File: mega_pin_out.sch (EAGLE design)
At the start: 11 parts, among them X1 332-36

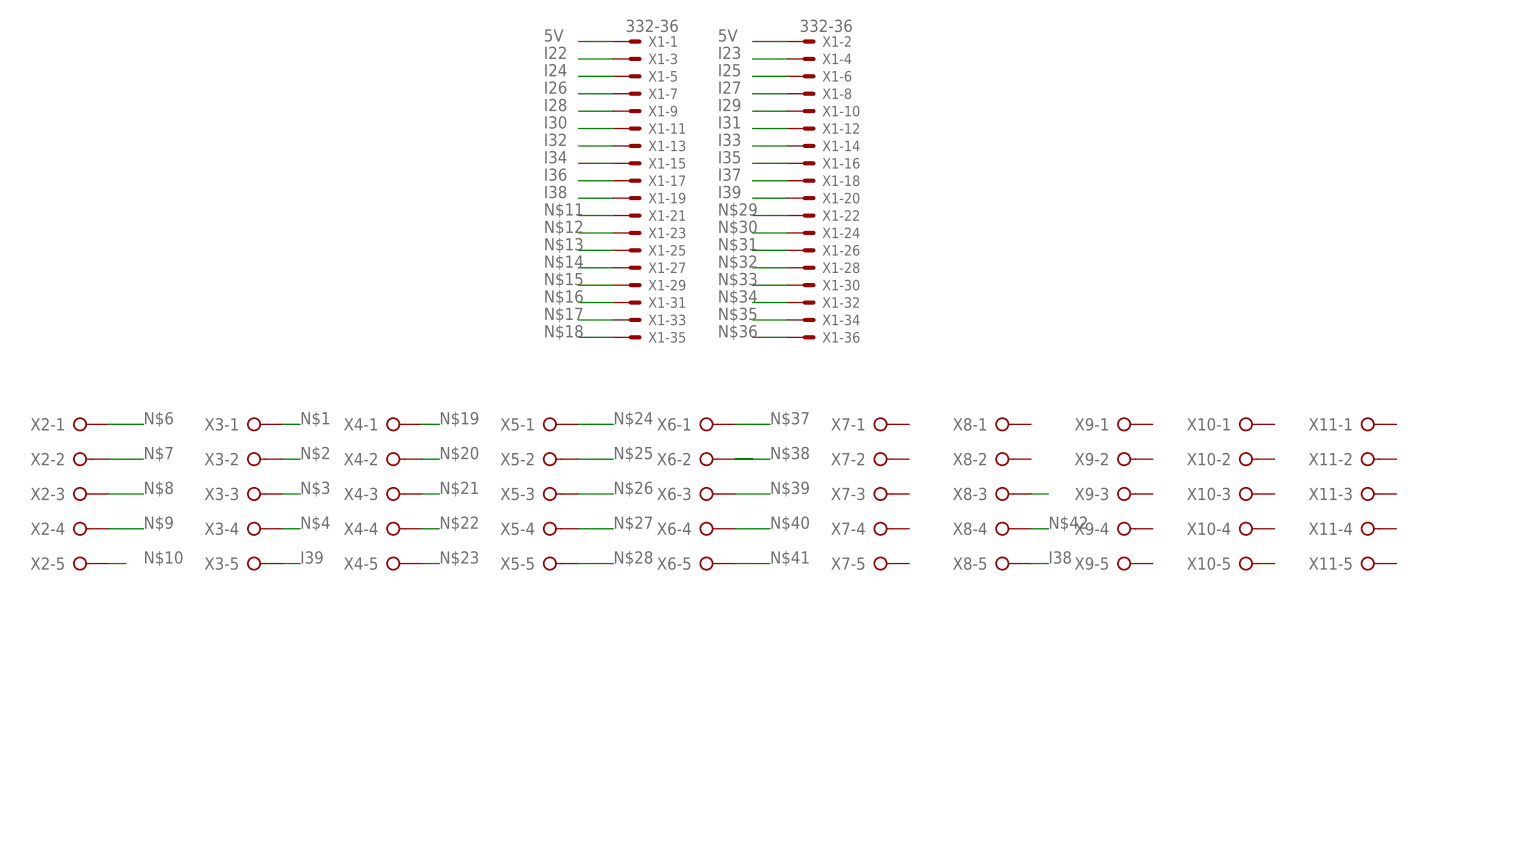
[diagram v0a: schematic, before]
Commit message: Full reroute of 2x18 female pins
- Fixed the female pins pcb layout part size
- Reroute all pins
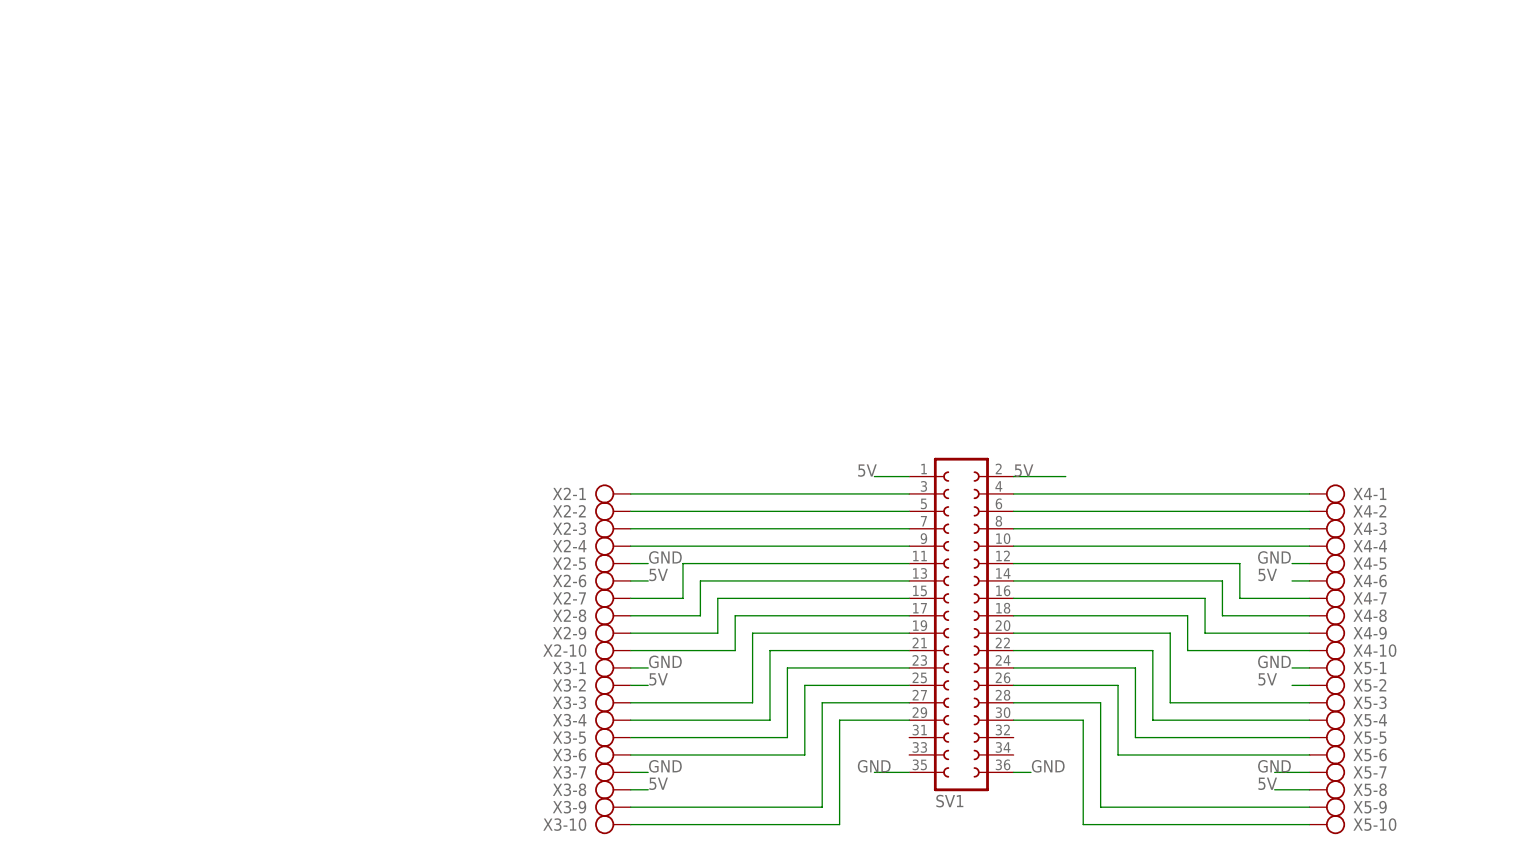
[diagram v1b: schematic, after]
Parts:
- removed X1: 332-36, con-garry:332-36
- removed X10, X11, X6, X7, X8, X9: (no value), con-wago-508:W237-05P
- added SV1: (no value), con-lsta:FE18-2
- X2, X3, X4, X5: device con-wago-508:W237-05P -> con-ptr500:AK500/10
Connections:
- removed net I22: X1-3.S
- removed net I23: X1-4.S
- removed net I24: X1-5.S
- removed net I25: X1-6.S
- removed net I26: X1-7.S
- removed net I27: X1-8.S
- removed net I28: X1-9.S
- removed net I29: X1-10.S
- removed net I30: X1-11.S
- removed net I32: X1-13.S
- removed net I34: X1-15.S
- removed net I36: X1-17.S
- removed net I37: X1-18.S
- removed net I38: X1-19.S, X8-5.KL
- removed net I39: X1-20.S, X3-5.KL
- removed net N$1: X3-1.KL
- removed net N$2: X3-2.KL
- removed net N$30: X1-24.S
- removed net N$31: X1-26.S
- removed net N$32: X1-28.S
- removed net N$33: X1-30.S
- removed net N$34: X1-32.S
- removed net N$35: X1-34.S
- removed net N$36: X1-36.S
- removed net N$37: X6-1.KL
- removed net N$38: X6-2.KL
- removed net N$39: X6-3.KL
- removed net N$40: X6-4.KL
- removed net N$41: X6-5.KL
- removed net N$42: X8-4.KL
- removed net N$43: X8-3.KL
- removed net N$6: X2-1.KL
- removed net N$7: X2-2.KL
- removed net N$8: X2-3.KL
- new net GND: SV1.35, SV1.36, X2-5.KL, X3-1.KL, X3-7.KL, X4-5.KL, X5-1.KL, X5-7.KL
- new net I47: SV1.27, X3-9.KL
- new net I49: SV1.29, X3-10.KL
- net 5V: now also SV1.1, SV1.2, X2-6.KL, X3-2.KL, X3-8.KL, X4-6.KL, X5-2.KL, X5-8.KL; no longer X1-1.S, X1-2.S
- net I31: now also SV1.11, X2-7.KL; no longer X1-12.S
- net I33: now also SV1.13, X2-8.KL; no longer X1-14.S
- net I35: now also SV1.15, X2-9.KL; no longer X1-16.S
- net N$10: now also SV1.9, X2-4.KL; no longer X2-5.KL
- net N$11: now also SV1.17, X2-10.KL; no longer X1-21.S
- net N$12: now also SV1.19, X3-3.KL; no longer X1-23.S
- net N$13: now also SV1.21, X3-4.KL; no longer X1-25.S
- net N$14: now also SV1.23, X3-5.KL; no longer X1-27.S
- net N$15: now also SV1.25, X3-6.KL; no longer X1-29.S
- net N$16: now also SV1.4, X4-1.KL; no longer X1-31.S
- net N$17: now also SV1.6, X4-2.KL; no longer X1-33.S
- net N$18: now also SV1.8, X4-3.KL; no longer X1-35.S
- net N$19: now also SV1.10, X4-4.KL; no longer X4-1.KL
- net N$20: now also SV1.12, X4-7.KL; no longer X4-2.KL
- net N$21: now also SV1.14, X4-8.KL; no longer X4-3.KL
- net N$22: now also SV1.16, X4-9.KL; no longer X4-4.KL
- net N$23: now also SV1.18, X4-10.KL; no longer X4-5.KL
- net N$24: now also SV1.20, X5-3.KL; no longer X5-1.KL
- net N$25: now also SV1.22, X5-4.KL; no longer X5-2.KL
- net N$26: now also SV1.24, X5-5.KL; no longer X5-3.KL
- net N$27: now also SV1.26, X5-6.KL; no longer X5-4.KL
- net N$28: now also SV1.28, X5-9.KL; no longer X5-5.KL
- net N$29: now also SV1.30, X5-10.KL; no longer X1-22.S
- net N$3: now also SV1.3, X2-1.KL; no longer X3-3.KL
- net N$4: now also SV1.5, X2-2.KL; no longer X3-4.KL
- net N$9: now also SV1.7, X2-3.KL; no longer X2-4.KL

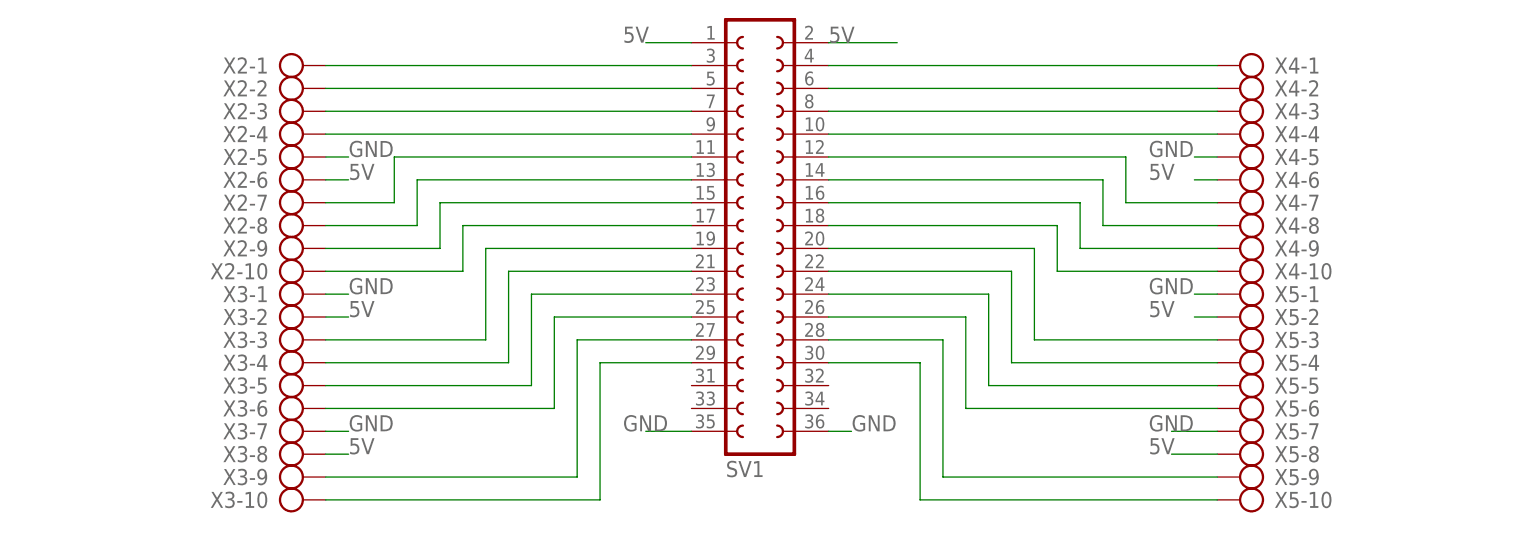
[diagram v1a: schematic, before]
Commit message: [BACK] Added capacitors for PIN 39 & 40 and others
* Schematic:
- Added text field for pin numbers name
- Added charging capacitors for pin 39 & 40 which are used as AC light state detectors. 

* Board
- Increased board layout from 100x80 to 100x85
- Increased clearance between terminal blocks to ~22.86 mm which was tested on breadboard to be easier during wiring. 
- Routed the capacitors
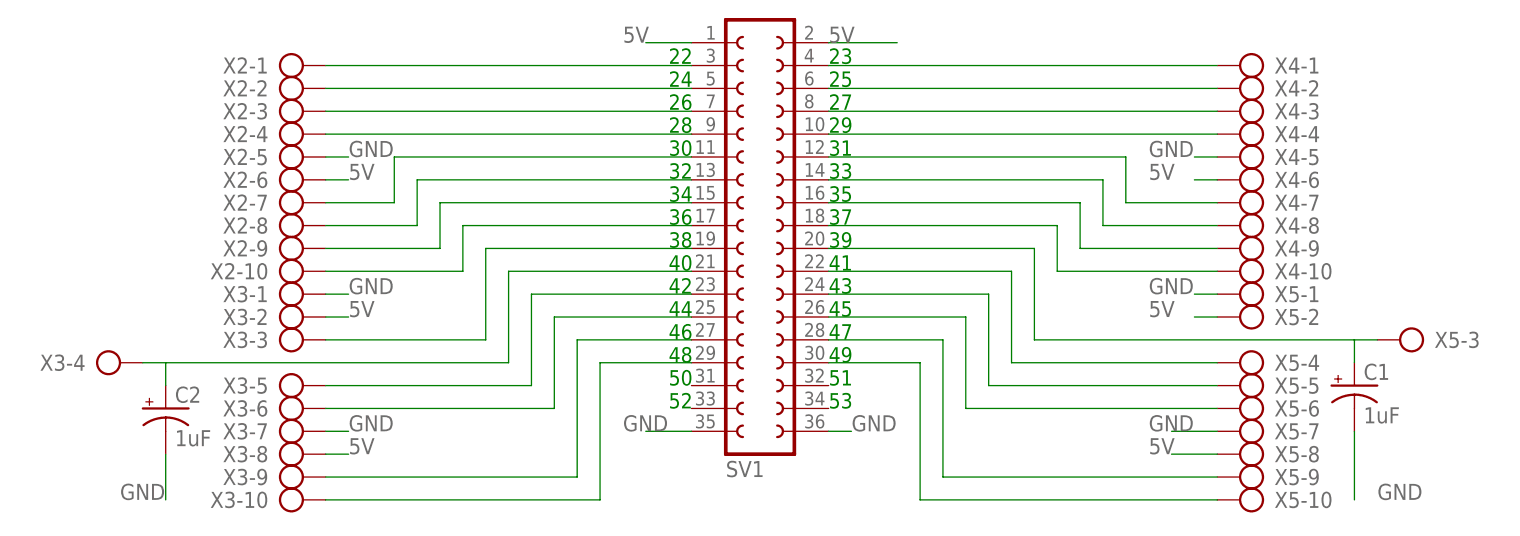
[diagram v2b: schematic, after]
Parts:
- added C1, C2: 1uF, adafruit:CPOL-USE2-4
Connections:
- net GND: now also C1.-, C2.-
- net N$13: now also C2.+
- net N$24: now also C1.+
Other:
- note added: "22 24 26 28 30 32 34 36 38 40 42 44 46 48 50 52"
- note added: "23 25 27 29 31 33 35 37 39 41 43 45 47 49 51 53"
- moved on the sheet: X3-4, X5-3
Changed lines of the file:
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@@
 <?xml version="1.0" encoding="utf-8"?>
 <!DOCTYPE eagle SYSTEM "eagle.dtd">
-<eagle version="7.7.0">
+<eagle version="7.3.0">
 <drawing>
 <settings>
@@
 <part name="X5" library="con-ptr500" deviceset="AK500/10" device=""/>
 <part name="SV1" library="con-lsta" deviceset="FE18-2" device=""/>
+<part name="C1" library="adafruit" deviceset="CPOL-US" device="E2-4" value="1uF"/>
+<part name="C2" library="adafruit" deviceset="CPOL-US" device="E2-4" value="1uF"/>
 </parts>
 <sheets>
 <sheet>
 <plain>
+<text x="142.24" y="-10.16" size="1.7018" layer="91">22
+24
+26
+28
+30
+32
+34
+36
+38
+40
+42
+44
+46
+48
+50
+52</text>
+<text x="160.02" y="-10.16" size="1.7018" layer="91">23
+25
+27
+29
+31
+33
+35
+37
+39
+41
+43
+45
+47
+49
+51
+53</text>
 </plain>
 <instances>
@@
 <instance part="X3" gate="-2" x="99.06" y="0"/>
 <instance part="X3" gate="-3" x="99.06" y="-2.54"/>
-<instance part="X3" gate="-4" x="99.06" y="-5.08"/>
+<instance part="X3" gate="-4" x="78.74" y="-5.08"/>
 <instance part="X3" gate="-5" x="99.06" y="-7.62"/>
 <instance part="X3" gate="-6" x="99.06" y="-10.16"/>
@@
 <instance part="X5" gate="-1" x="208.28" y="2.54" rot="MR0"/>
 <instance part="X5" gate="-2" x="208.28" y="0" rot="MR0"/>
-<instance part="X5" gate="-3" x="208.28" y="-2.54" rot="MR0"/>
+<instance part="X5" gate="-3" x="226.06" y="-2.54" rot="MR0"/>
 <instance part="X5" gate="-4" x="208.28" y="-5.08" rot="MR0"/>
 <instance part="X5" gate="-5" x="208.28" y="-7.62" rot="MR0"/>
@@
 <instance part="X5" gate="-10" x="208.28" y="-20.32" rot="MR0"/>
 <instance part="SV1" gate="G$1" x="152.4" y="7.62" rot="MR180"/>
+<instance part="C1" gate="G$1" x="218.44" y="-7.62"/>
+<instance part="C2" gate="G$1" x="86.36" y="-10.16"/>
 </instances>
 <busses>
@@
 <label x="195.58" y="-12.7" size="1.778" layer="95"/>
 </segment>
+<segment>
+<pinref part="C1" gate="G$1" pin="-"/>
+<wire x1="218.44" y1="-12.7" x2="218.44" y2="-20.32" width="0.1524" layer="91"/>
+<label x="220.98" y="-20.32" size="1.778" layer="95"/>
+</segment>
+<segment>
+<pinref part="C2" gate="G$1" pin="-"/>
+<wire x1="86.36" y1="-15.24" x2="86.36" y2="-20.32" width="0.1524" layer="91"/>
+<label x="81.28" y="-20.32" size="1.778" layer="95"/>
+</segment>
 </net>
 <net name="I31" class="0">
@@
 <wire x1="124.46" y1="5.08" x2="124.46" y2="-5.08" width="0.1524" layer="91"/>
 <pinref part="X3" gate="-4" pin="KL"/>
-<wire x1="124.46" y1="-5.08" x2="104.14" y2="-5.08" width="0.1524" layer="91"/>
+<wire x1="124.46" y1="-5.08" x2="86.36" y2="-5.08" width="0.1524" layer="91"/>
 <pinref part="SV1" gate="G$1" pin="21"/>
+<wire x1="86.36" y1="-5.08" x2="83.82" y2="-5.08" width="0.1524" layer="91"/>
 <wire x1="144.78" y1="5.08" x2="124.46" y2="5.08" width="0.1524" layer="91"/>
+<pinref part="C2" gate="G$1" pin="+"/>
+<wire x1="86.36" y1="-7.62" x2="86.36" y2="-5.08" width="0.1524" layer="91"/>
 </segment>
 </net>
@@
 <segment>
 <pinref part="X5" gate="-3" pin="KL"/>
-<wire x1="203.2" y1="-2.54" x2="182.88" y2="-2.54" width="0.1524" layer="91"/>
+<wire x1="220.98" y1="-2.54" x2="218.44" y2="-2.54" width="0.1524" layer="91"/>
+<wire x1="218.44" y1="-2.54" x2="182.88" y2="-2.54" width="0.1524" layer="91"/>
 <wire x1="182.88" y1="-2.54" x2="182.88" y2="7.62" width="0.1524" layer="91"/>
 <pinref part="SV1" gate="G$1" pin="20"/>
 <wire x1="182.88" y1="7.62" x2="160.02" y2="7.62" width="0.1524" layer="91"/>
+<pinref part="C1" gate="G$1" pin="+"/>
+<wire x1="218.44" y1="-5.08" x2="218.44" y2="-2.54" width="0.1524" layer="91"/>
 </segment>
 </net>
@@
 </schematic>
 </drawing>
+<compatibility>
+<note version="6.3" minversion="6.2.2" severity="warning">
+Since Version 6.2.2 text objects can contain more than one line,
+which will not be processed correctly with this version.
+</note>
+</compatibility>
 </eagle>

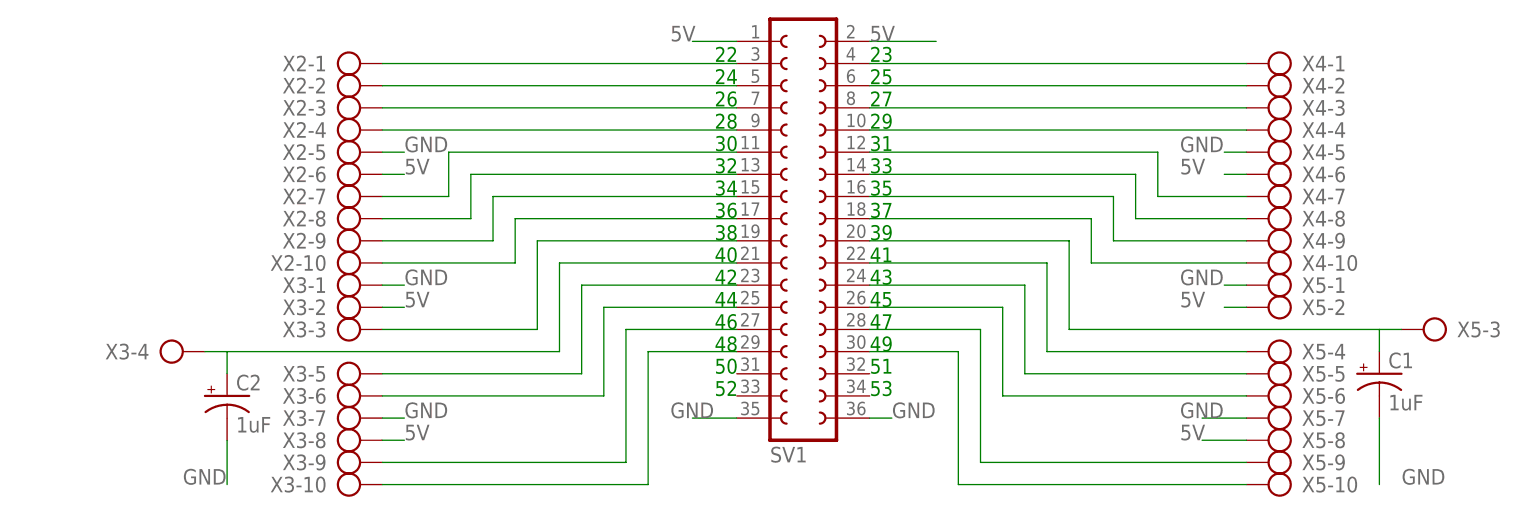
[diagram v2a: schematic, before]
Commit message: [BUG][MAJOR] Fix wrong orientation of pin header
- Pin header connections were all wrong and mirrored. To fix it, I mirrored the header in schematics and rerouted the wrong pins.
- Added labels
- increased the distance between the two terminal block rows to ~31 cm
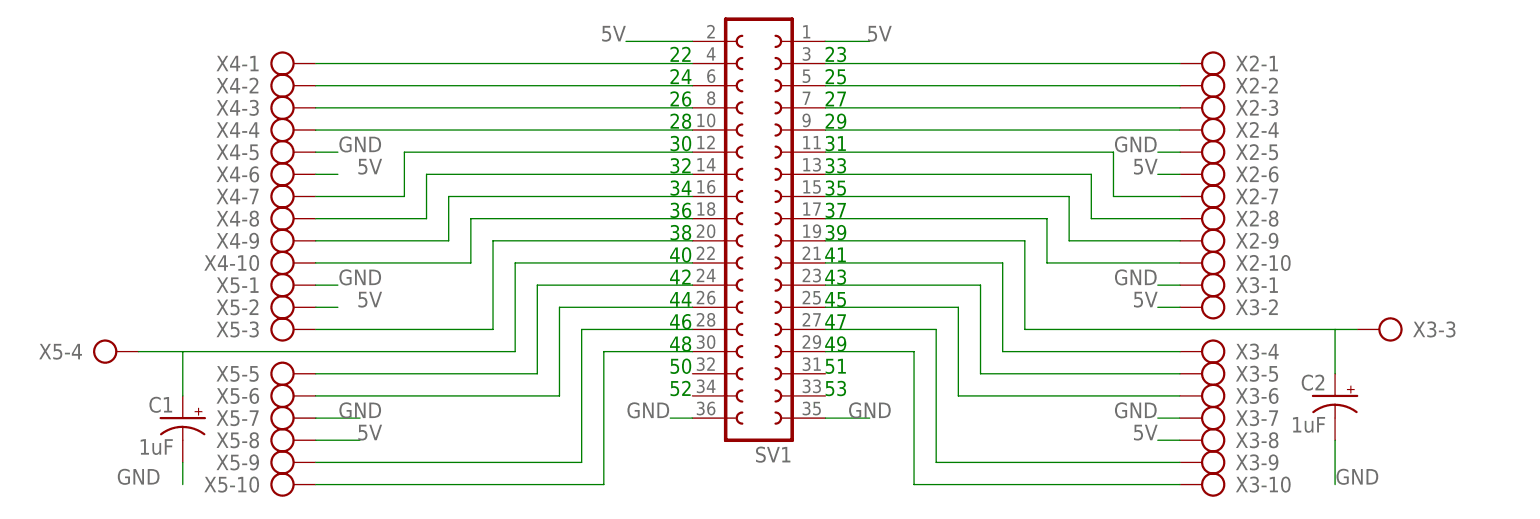
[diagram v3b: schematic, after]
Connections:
- removed net N$12: SV1.19, X3-3.KL
- removed net N$25: SV1.22, X5-4.KL
- new net N$1: C2.+, SV1.19, X3-3.KL
- new net N$2: SV1.20, X5-3.KL
- net N$13: no longer C2.+
- net N$24: now also SV1.22, X5-4.KL; no longer SV1.20, X5-3.KL
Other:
- moved on the sheet: C1, C2, SV1, X2-1, X2-10, X2-2, X2-3, X2-4, X2-5, X2-6, X2-7, X2-8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
